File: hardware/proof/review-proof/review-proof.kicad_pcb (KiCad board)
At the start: 4 copper layers, 92 x 60 mm, 26 parts, among them J1 MAINS, J2 5V_IN, J4 LOAD, U1 VO3526, U2 AMS1117-3.3, U3 MCP6001-OT, U4 ATtiny85-20M, Y1 8MHz

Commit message: fix(hardware): seat the crystal's load capacitors at U4's pins, part AMP_OUT from the 3V3 route, and return R3 at the shunt [SOL-BOARD-LAYOUT-WORKMANSHIP-ITEMS.C3, .C4]
The tidy had pushed C5 and C6 to the crystal's two ends, 16.6 mm apart, run
XTAL1 and XTAL2 side by side for 5.3 mm, laid AMP_OUT 0.66 mm under the +3V3
diagonal for 7 mm, moved R3's ground 12.4 mm from the shunt inside the
ground pour, and turned AMP_FB square through R2's pad. C5 and C6 now sit
side by side on their own pins' tracks with the crystal turned beyond them
and its tracks parting at once; AMP_OUT crosses the +3V3 route once and
branches at U3's pin-1 via; R2 is entered at 45 degrees and passes straight
on to R3; and R3's return runs by its own track to R1's ground pad through a
rule area that keeps the pour off it. Tracks and parts go through Konnect;
the three vias left unused and the rule area, which Konnect cannot make,
through KiCad's own scripting on the closed board, which refilled and saved
it. The stub figure leaves the project, the plan and rules table follow the
board, and the seeds on the moved copper are re-anchored, the stub seed now
taking out its rules-table row as the via seed does.

Co-Authored-By: Claude Opus 5.5 (1M context) <noreply@anthropic.com>
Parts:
- moved C5 8.29 mm to (75.6, 15.3)
- moved C6 7.87 mm to (75.6, 12.2)
- moved Y1 4.03 mm to (84.0, 14.5), turned to 0 degrees
- moved R2 1.42 mm to (72.4, 46.4)
- moved R3 0.10 mm to (70.8, 47.9)
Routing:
- net /XTAL1: track 12.6 -> 5.08 mm
- net /XTAL2: track 12.1 -> 14.4 mm
- net /AMP_OUT: track 44.8 -> 43.1 mm
- net /AMP_FB: track 5.29 -> 4.55 mm
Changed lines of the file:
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@@
 	(property "WORK_PAD_ANGLE_DEG" "90")
 	(property "WORK_PAD_ENTRY_RATIO" "2")
-	(property "WORK_STUB_MM" "0")
 	(footprint "Package_TO_SOT_SMD:SOT-223-3_TabPin2"
 		(layer "F.Cu")
@@
 	(footprint "Resistor_SMD:R_0603_1608Metric"
 		(layer "F.Cu")
-		(at 72.4 44.95 180)
+		(at 72.4 46.375 180)
 		(descr "Resistor SMD 0603 (1608 Metric), square (rectangular) end terminal, IPC-7351 nominal, (Body size source: IPC-SM-782 page 72, https://www.pcb-3d.com/wordpress/wp-content/uploads/ipc-sm-782a_amendment_1_and_2.pdf)")
 		(tags "resistor")
 		(property "Reference" "R2"
-			(at 0 -1.43 180)
+			(at -3.2 0 0)
 			(layer "F.SilkS")
 			(effects
@@
 	(footprint "Crystal:Crystal_SMD_HC49-SD"
 		(layer "F.Cu")
-		(at 80 14 90)
+		(at 84 14.5)
 		(descr "HC-49-SD, Crystal, 11.4x4.7mm package, SMD, http://cdn-reichelt.de/documents/datenblatt/B400/xxx-HC49-SMD.pdf")
 		(property "Reference" "Y1"
-			(at 0 -3.55 90)
+			(at 0 -3.55 0)
 			(layer "F.SilkS")
 			(effects
@@
 		)
 		(property "Value" "8MHz"
-			(at 0.5 3.55 90)
+			(at 0.5 3.55 0)
 			(layer "F.Fab")
 			(effects
@@
 		)
 		(property "Datasheet" ""
-			(at 0 0 90)
+			(at 0 0 0)
 			(layer "F.Fab")
 			(hide yes)
@@
 		)
 		(property "Description" "Two pin crystal"
-			(at 0 0 90)
+			(at 0 0 0)
 			(layer "F.Fab")
 			(hide yes)
@@
 		)
 		(property "KiLib_Generator" "crystal_resonator_oscillator"
-			(at 0 0 90)
+			(at 0 0 0)
 			(layer "F.SilkS")
 			(hide yes)
@@
 		(duplicate_pad_numbers_are_jumpers no)
 		(fp_line
-			(start 5.96 -2.61)
-			(end -6.76 -2.61)
+			(start -6.76 -2.61)
+			(end -6.76 2.61)
 			(stroke
 				(width 0.12)
@@
 		)
 		(fp_line
-			(start -6.76 -2.61)
-			(end -6.76 2.61)
+			(start -6.76 2.61)
+			(end 5.96 2.61)
 			(stroke
 				(width 0.12)
@@
 		)
 		(fp_line
-			(start -6.76 2.61)
-			(end 5.96 2.61)
+			(start 5.96 -2.61)
+			(end -6.76 -2.61)
 			(stroke
 				(width 0.12)
@@
 		)
 		(fp_arc
-			(start 3.35 -1.88)
-			(mid 5.23 0)
-			(end 3.35 1.88)
+			(start -3.35 1.88)
+			(mid -5.23 0)
+			(end -3.35 -1.88)
 			(stroke
 				(width 0.1)
@@
 		)
 		(fp_arc
-			(start -3.35 1.88)
-			(mid -5.23 0)
-			(end -3.35 -1.88)
+			(start 3.35 -1.88)
+			(mid 5.23 0)
+			(end 3.35 1.88)
 			(stroke
 				(width 0.1)
@@
 		)
 		(fp_text user "${REFERENCE}"
-			(at 0 0 90)
+			(at 0 0 0)
 			(layer "F.Fab")
 			(effects
@@
 		)
 		(pad "1" smd roundrect
-			(at -4.25 0 90)
+			(at -4.25 0)
 			(size 4.5 2)
 			(layers "F.Cu" "F.Mask" "F.Paste")
@@
 		)
 		(pad "2" smd roundrect
-			(at 4.25 0 90)
+			(at 4.25 0)
 			(size 4.5 2)
 			(layers "F.Cu" "F.Mask" "F.Paste")
@@
 	(footprint "Resistor_SMD:R_0603_1608Metric"
 		(layer "F.Cu")
-		(at 70.75 47.8 180)
+		(at 70.75 47.9 180)
 		(descr "Resistor SMD 0603 (1608 Metric), square (rectangular) end terminal, IPC-7351 nominal, (Body size source: IPC-SM-782 page 72, https://www.pcb-3d.com/wordpress/wp-content/uploads/ipc-sm-782a_amendment_1_and_2.pdf)")
 		(tags "resistor")
@@
 	(footprint "Capacitor_SMD:C_0603_1608Metric"
 		(layer "F.Cu")
-		(at 80 5.7 90)
+		(at 75.6 12.225 90)
 		(descr "Capacitor SMD 0603 (1608 Metric), square (rectangular) end terminal, IPC-7351 nominal, (Body size source: IPC-SM-782 page 76, https://www.pcb-3d.com/wordpress/wp-content/uploads/ipc-sm-782a_amendment_1_and_2.pdf)")
 		(tags "capacitor")
 		(property "Reference" "C6"
-			(at 0 -1.43 90)
+			(at 3.725 0 0)
 			(layer "F.SilkS")
 			(effects
@@
 	(footprint "Capacitor_SMD:C_0603_1608Metric"
 		(layer "F.Cu")
-		(at 80 22.3 -90)
+		(at 75.6 15.275 -90)
 		(descr "Capacitor SMD 0603 (1608 Metric), square (rectangular) end terminal, IPC-7351 nominal, (Body size source: IPC-SM-782 page 76, https://www.pcb-3d.com/wordpress/wp-content/uploads/ipc-sm-782a_amendment_1_and_2.pdf)")
 		(tags "capacitor")
 		(property "Reference" "C5"
-			(at 0 -1.43 270)
+			(at 3.725 0 0)
 			(layer "F.SilkS")
 			(effects
@@
 	)
 	(segment
-		(start 80 23.075)
-		(end 80 24.3)
+		(start 69.925 47.9)
+		(end 64.0625 47.9)
 		(width 0.5)
 		(layer "F.Cu")
@@
 	)
 	(segment
-		(start 62.9625 51)
-		(end 62.9625 54)
+		(start 62.9625 49)
+		(end 62.9625 51)
 		(width 0.5)
 		(layer "F.Cu")
@@
 	)
 	(segment
-		(start 39.1 9.2)
-		(end 40.3 9.2)
+		(start 62.9625 51)
+		(end 62.9625 54)
 		(width 0.5)
 		(layer "F.Cu")
@@
 	)
 	(segment
-		(start 62.9625 49.2)
-		(end 62.9625 51)
+		(start 75.6 16.05)
+		(end 75.6 17.4)
 		(width 0.5)
 		(layer "F.Cu")
@@
 	)
 	(segment
-		(start 64.3625 47.8)
-		(end 62.9625 49.2)
+		(start 39.1 9.2)
+		(end 40.3 9.2)
 		(width 0.5)
 		(layer "F.Cu")
@@
 	)
 	(segment
-		(start 69.925 47.8)
-		(end 64.3625 47.8)
+		(start 75.6 11.45)
+		(end 75.6 10.1)
 		(width 0.5)
 		(layer "F.Cu")
@@
 	)
 	(segment
-		(start 80 4.925)
-		(end 80 3.7)
+		(start 64.0625 47.9)
+		(end 62.9625 49)
 		(width 0.5)
 		(layer "F.Cu")
@@
 	)
 	(via
-		(at 80 24.3)
-		(size 0.9)
-		(drill 0.35)
-		(layers "F.Cu" "B.Cu")
-		(net "/GND")
-	)
-	(via
 		(at 72.65 13.35)
 		(size 0.82)
@@
 	)
 	(via
+		(at 75.6 10.1)
+		(size 0.9)
+		(drill 0.35)
+		(layers "F.Cu" "B.Cu")
+		(net "/GND")
+	)
+	(via
 		(at 72.65 14.65)
 		(size 0.82)
@@
 	)
 	(via
-		(at 80 3.7)
-		(size 0.9)
-		(drill 0.35)
-		(layers "F.Cu" "B.Cu")
-		(net "/GND")
-	)
-	(via
 		(at 35.325 23)
 		(size 0.9)
@@
 	)
 	(via
+		(at 75.6 17.4)
+		(size 0.9)
+		(drill 0.35)
+		(layers "F.Cu" "B.Cu")
+		(net "/GND")
+	)
+	(via
 		(at 69.5 55.5)
 		(size 0.9)
@@
 	)
 	(segment
-		(start 73.225 43.45)
-		(end 73.225 44.95)
+		(start 73.225 45.3)
+		(end 73.225 46.375)
 		(width 0.25)
 		(layer "F.Cu")
@@
 	)
 	(via
-		(at 73.225 43.45)
+		(at 73.225 45.3)
 		(size 0.9)
 		(drill 0.35)
@@
 	)
 	(segment
-		(start 68.25 14.5)
-		(end 68.25 33)
+		(start 66.7 44.45)
+		(end 72.375 44.45)
 		(width 0.25)
 		(layer "B.Cu")
@@
 	)
 	(segment
-		(start 73.225 37.975)
-		(end 73.225 43.45)
+		(start 68.25 14.5)
+		(end 68.25 38.5)
 		(width 0.25)
 		(layer "B.Cu")
@@
 	)
 	(segment
-		(start 73.225 43.45)
-		(end 72.225 44.45)
+		(start 68.25 38.5)
+		(end 65.3 41.45)
 		(width 0.25)
 		(layer "B.Cu")
@@
 	)
 	(segment
-		(start 72.225 44.45)
-		(end 66.7 44.45)
+		(start 66.7 44.45)
+		(end 65.3 43.05)
 		(width 0.25)
 		(layer "B.Cu")
@@
 	)
 	(segment
-		(start 66.7 44.45)
+		(start 65.3 41.45)
 		(end 65.3 43.05)
 		(width 0.25)
@@
 	)
 	(segment
-		(start 68.25 33)
-		(end 73.225 37.975)
+		(start 72.375 44.45)
+		(end 73.225 45.3)
 		(width 0.25)
 		(layer "B.Cu")
@@
 	)
 	(segment
-		(start 71.575 44.95)
-		(end 71.575 47.8)
+		(start 70.15 44.95)
+		(end 71.575 46.375)
 		(width 0.25)
 		(layer "F.Cu")
@@
 	)
 	(segment
-		(start 69.1375 44.95)
-		(end 71.575 44.95)
+		(start 71.575 46.375)
+		(end 71.575 47.9)
 		(width 0.25)
 		(layer "F.Cu")
@@
 	)
 	(segment
-		(start 80 15.3)
-		(end 80 18.25)
+		(start 69.1375 44.95)
+		(end 70.15 44.95)
 		(width 0.25)
 		(layer "F.Cu")
-		(net "/XTAL1")
+		(net "/AMP_FB")
 	)
 	(segment
-		(start 79.2 14.5)
-		(end 80 15.3)
+		(start 75.6 14.5)
+		(end 79 14.5)
 		(width 0.25)
 		(layer "F.Cu")
@@
 	)
 	(segment
-		(start 80 18.25)
-		(end 80 21.525)
+		(start 73.925 14.5)
+		(end 75.6 14.5)
 		(width 0.25)
 		(layer "F.Cu")
@@
 	)
 	(segment
-		(start 73.925 14.5)
-		(end 79.2 14.5)
+		(start 85 14.5)
+		(end 86.5 14.5)
 		(width 0.25)
 		(layer "F.Cu")
-		(net "/XTAL1")
+		(net "/XTAL2")
 	)
 	(segment
 		(start 73.925 13)
-		(end 79.2 13)
+		(end 75.6 13)
 		(width 0.25)
 		(layer "F.Cu")
@@
 	)
 	(segment
-		(start 80 12.2)
-		(end 80 9.75)
+		(start 75.6 13)
+		(end 76.6 13)
 		(width 0.25)
 		(layer "F.Cu")
@@
 	)
 	(segment
-		(start 79.2 13)
-		(end 80 12.2)
+		(start 82 11.5)
+		(end 85 14.5)
 		(width 0.25)
 		(layer "F.Cu")
@@
 	)
 	(segment
-		(start 80 9.75)
-		(end 80 6.475)
+		(start 78.1 11.5)
+		(end 82 11.5)
+		(width 0.25)
+		(layer "F.Cu")
+		(net "/XTAL2")
+	)
+	(segment
+		(start 76.6 13)
+		(end 78.1 11.5)
 		(width 0.25)
 		(layer "F.Cu")
@@
 			)
 		)
+	)
+	(zone
+		(layer "F.Cu")
+		(name "R3 ground return")
+		(hatch edge 0.5)
+		(connect_pads
+			(clearance 0)
+		)
+		(min_thickness 0.25)
+		(keepout
+			(tracks allowed)
+			(vias allowed)
+			(pads allowed)
+			(copperpour not_allowed)
+			(footprints allowed)
+		)
+		(placement
+			(enabled no)
+			(sheetname "")
+		)
+		(fill
+			(thermal_gap 0.5)
+			(thermal_bridge_width 0.5)
+			(island_removal_mode 0)
+		)
+		(polygon
+			(pts
+				(xy 70.6 47.3) (xy 70.6 48.5) (xy 64.709999 48.5) (xy 64.01 49.2) (xy 62.3 49.2) (xy 64.2 47.3)
+			)
+		)

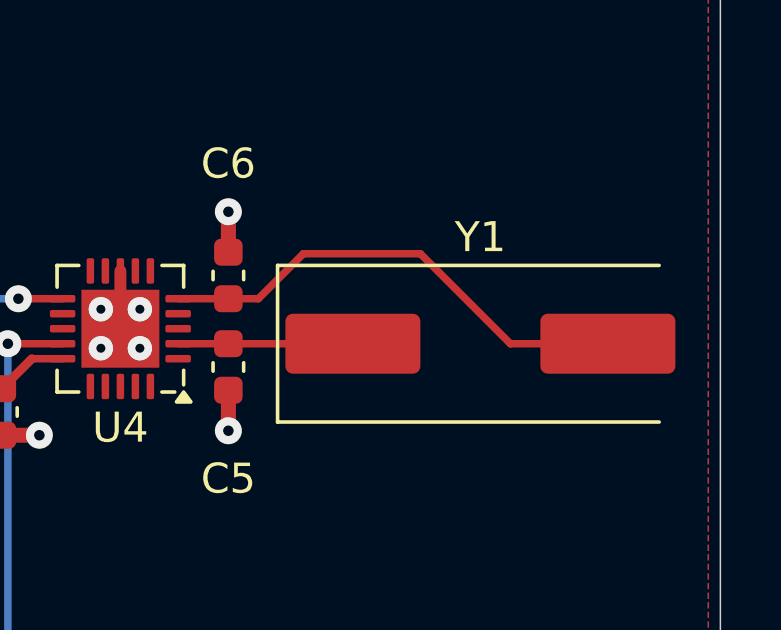
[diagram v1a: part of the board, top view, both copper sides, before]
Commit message: fix(hardware): fit a two-pad crystal whose pads face its capacitors, and keep the R3 rule area clear of its track [SOL-BOARD-LAYOUT-WORKMANSHIP-ITEMS.C3, .C4]
Round 4 finding 4.1: the HC49-SD crystal's pads lie 8.5 mm apart and each
must be entered along its length, so no way of turning it both keeps its two
tracks apart (CLOCK-1) and faces each pad to its capacitor (WORK-1). Y1 is
now a 5.0 by 3.2 mm two-pad crystal from KiCad's own library, its schematic
footprint field changed with it, set just beyond C5 and C6 with each pad
facing its capacitor and both tracks 5.7 mm long; it sits 25.1 mm from C2's
body, so no further part comes within CLOCK-3's 25 mm. The footprint is
swapped with KiCad's own scripting on the closed board, keeping its symbol
link and nets, since Konnect cannot change a placed footprint; the tracks
and placement go through Konnect.

Round 4 finding 4.2: the R3 ground return rule area is redrawn to follow
the track's 45-degree run, so the pour stops 0.35 mm or more from the track and 0.275 mm from R3's pad
everywhere rather than 0.077 mm.

The plan, the rules table and the crystal seeds follow.

Co-Authored-By: Claude Opus 5.5 (1M context) <noreply@anthropic.com>
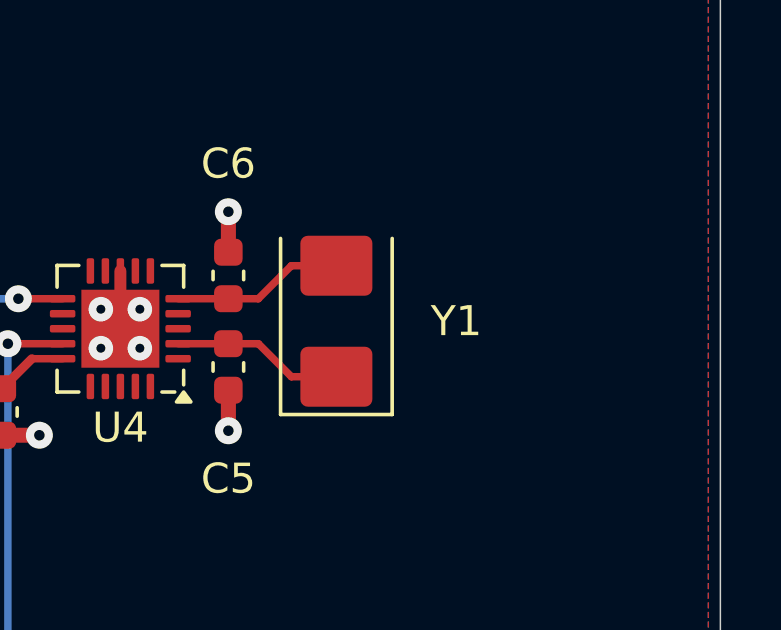
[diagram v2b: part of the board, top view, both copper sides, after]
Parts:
- Y1: footprint Crystal:Crystal_SMD_HC49-SD -> Crystal:Crystal_SMD_5032-2Pin_5.0x3.2mm
- moved Y1 4.86 mm to (79.2, 13.8), turned to 90 degrees
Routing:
- net /XTAL2: track 14.4 -> 5.73 mm
- net /XTAL1: track 5.08 -> 5.73 mm
